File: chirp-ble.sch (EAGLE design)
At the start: 29 parts, among them Q1 ILCX13-FF5F18-32.0000, U1 NRF52832, Y1 ABS07-32.768KHZ-7

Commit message: Fully routed
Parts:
- added TP4: TPB1,27, testpad:TPB1,27
- Q1: value ILCX13-FF5F18-32.0000 -> ILCX13-FF5F18-32.0000
- S1: value SWITCH-MOMENTARY-2-SMD-1101NE -> SWITCH-MOMENTARY-2SMD-1101NE; device SparkFun-Electromechanical:SWITCH-MOMENTARY-2-SMD-1101NE -> SparkFun-Electromechanical:SWITCH-MOMENTARY-2SMD-1101NE
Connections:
- net LED renamed LED_K
- removed net N$14: SWD.SWO
- removed net N$5: SWD.VTREF
- new net LED_A: LED1.A, U1.NFC2/P0.10
- net GND: now also Q1.G1, Q1.G2, TP4.TP, U1.VSS@3
- net VCC: now also SWD.VTREF; no longer LED1.A
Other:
- moved on the sheet: ANTENNA, C1, C10, C11, C12, C13, C2, C3, C5, C6, C7, C8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

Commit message: DRC and ERC
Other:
- moved on the sheet: C9
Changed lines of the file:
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@@
 </instance>
 <instance part="GND8" gate="1" x="152.4" y="43.18"/>
-<instance part="C9" gate="G$1" x="139.7" y="22.86" rot="MR180"/>
+<instance part="C9" gate="G$1" x="147.32" y="22.86" rot="MR180"/>
 <instance part="C10" gate="G$1" x="170.18" y="66.04" smashed="yes" rot="MR270">
 <attribute name="NAME" x="173.736" y="71.501" size="1.778" layer="95" rot="MR0"/>
@@
 <attribute name="NAME" x="183.642" y="20.32" size="1.778" layer="95" rot="MR90"/>
 </instance>
-<instance part="GND10" gate="1" x="139.7" y="15.24"/>
-<instance part="GND11" gate="1" x="170.18" y="17.78"/>
+<instance part="GND10" gate="1" x="147.32" y="15.24"/>
+<instance part="GND11" gate="1" x="170.18" y="15.24"/>
 <instance part="GND13" gate="1" x="177.8" y="45.72"/>
 <instance part="GND16" gate="1" x="127" y="10.16" rot="R90"/>
@@
 <pinref part="GND10" gate="1" pin="GND"/>
 <pinref part="C9" gate="G$1" pin="1"/>
-<wire x1="139.7" y1="17.78" x2="139.7" y2="20.32" width="0.1524" layer="91"/>
+<wire x1="147.32" y1="17.78" x2="147.32" y2="20.32" width="0.1524" layer="91"/>
 </segment>
 <segment>
@@
 <pinref part="GND11" gate="1" pin="GND"/>
 <wire x1="175.26" y1="25.4" x2="170.18" y2="25.4" width="0.1524" layer="91"/>
-<wire x1="170.18" y1="25.4" x2="170.18" y2="20.32" width="0.1524" layer="91"/>
+<wire x1="170.18" y1="25.4" x2="170.18" y2="17.78" width="0.1524" layer="91"/>
 </segment>
 <segment>
@@
 <wire x1="124.46" y1="45.72" x2="132.08" y2="45.72" width="0.1524" layer="91"/>
 <wire x1="132.08" y1="45.72" x2="132.08" y2="43.18" width="0.1524" layer="91"/>
-<wire x1="132.08" y1="43.18" x2="139.7" y2="43.18" width="0.1524" layer="91"/>
-<wire x1="139.7" y1="43.18" x2="139.7" y2="27.94" width="0.1524" layer="91"/>
+<wire x1="132.08" y1="43.18" x2="147.32" y2="43.18" width="0.1524" layer="91"/>
+<wire x1="147.32" y1="43.18" x2="147.32" y2="27.94" width="0.1524" layer="91"/>
 <pinref part="C9" gate="G$1" pin="2"/>
-<wire x1="139.7" y1="27.94" x2="154.94" y2="27.94" width="0.1524" layer="91"/>
-<junction x="139.7" y="27.94"/>
+<wire x1="147.32" y1="27.94" x2="154.94" y2="27.94" width="0.1524" layer="91"/>
+<junction x="147.32" y="27.94"/>
 <pinref part="L1" gate="G$1" pin="1"/>
 </segment>
@@
 <pinref part="U1" gate="G$1" pin="SWDCLK"/>
 <wire x1="124.46" y1="33.02" x2="129.54" y2="33.02" width="0.1524" layer="91"/>
-<label x="124.46" y="33.02" size="1.27" layer="95"/>
+<label x="129.54" y="33.02" size="1.27" layer="95" xref="yes"/>
 </segment>
 </net>
@@
 <pinref part="U1" gate="G$1" pin="SWDIO"/>
 <wire x1="124.46" y1="35.56" x2="129.54" y2="35.56" width="0.1524" layer="91"/>
-<label x="124.46" y="35.56" size="1.27" layer="95"/>
+<label x="129.54" y="35.56" size="1.27" layer="95" xref="yes"/>
 </segment>
 </net>
@@
 <pinref part="U1" gate="G$1" pin="P0.21/RESET"/>
 <wire x1="104.14" y1="15.24" x2="104.14" y2="10.16" width="0.1524" layer="91"/>
+<wire x1="104.14" y1="10.16" x2="106.68" y2="10.16" width="0.1524" layer="91"/>
+<label x="106.68" y="10.16" size="1.27" layer="95" xref="yes"/>
 </segment>
 </net>
@@
 <segment>
 <pinref part="U1" gate="G$1" pin="P0.13"/>
-<wire x1="83.82" y1="15.24" x2="83.82" y2="7.62" width="0.1524" layer="91"/>
-<label x="83.82" y="7.62" size="1.778" layer="95" rot="R90"/>
+<wire x1="83.82" y1="15.24" x2="83.82" y2="10.16" width="0.1524" layer="91"/>
+<label x="83.82" y="10.16" size="1.27" layer="95" rot="R270" xref="yes"/>
 </segment>
 </net>
@@
 <segment>
 <pinref part="U1" gate="G$1" pin="P0.28/AIN4"/>
-<wire x1="96.52" y1="81.28" x2="96.52" y2="93.98" width="0.1524" layer="91"/>
-<label x="96.52" y="83.82" size="1.778" layer="95" rot="R90"/>
+<wire x1="96.52" y1="81.28" x2="96.52" y2="86.36" width="0.1524" layer="91"/>
+<label x="96.52" y="86.36" size="1.27" layer="95" rot="R90" xref="yes"/>
 </segment>
 </net>
@@
 <segment>
 <pinref part="U1" gate="G$1" pin="P0.26"/>
-<wire x1="101.6" y1="81.28" x2="101.6" y2="93.98" width="0.1524" layer="91"/>
+<wire x1="101.6" y1="81.28" x2="101.6" y2="86.36" width="0.1524" layer="91"/>
+<label x="101.6" y="86.36" size="1.27" layer="95" rot="R90" xref="yes"/>
 </segment>
 </net>
@@
 <segment>
 <pinref part="U1" gate="G$1" pin="P0.17"/>
-<wire x1="93.98" y1="15.24" x2="93.98" y2="2.54" width="0.1524" layer="91"/>
-<label x="93.98" y="5.08" size="1.778" layer="95" rot="R90"/>
-</segment>
-</net>
+<wire x1="93.98" y1="15.24" x2="93.98" y2="10.16" width="0.1524" layer="91"/>
+<label x="93.98" y="10.16" size="1.27" layer="95" rot="R270" xref="yes"/>
+</segment>
+</net>

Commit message: Spike
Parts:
- Q1: value ILCX13-FF5F18-32.0000 -> YIC 32.00M-SMDXT324
- Y1: value ABS07-32.768KHZ-7 -> 32.768K-CFPX217
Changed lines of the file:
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@@
 <layer number="251" name="SMDround" color="12" fill="11" visible="no" active="no"/>
 <layer number="254" name="cooling" color="7" fill="1" visible="no" active="yes"/>
+<layer number="255" name="routoute" color="7" fill="1" visible="yes" active="yes"/>
 </layers>
 <schematic xreflabel="%F%N/%S.%C%R" xrefpart="/%S.%C%R">
@@
 <part name="C13" library="rcl" deviceset="C-EU" device="C0402" value="12pF"/>
 <part name="FRAME1" library="frames" deviceset="A4L-LOC" device=""/>
-<part name="Y1" library="abracon" deviceset="CRYSTAL" device=".ABS07" value="ABS07-32.768KHZ-7 "/>
+<part name="Y1" library="abracon" deviceset="CRYSTAL" device=".ABS07" value="32.768K-CFPX217"/>
 <part name="GND9" library="SparkFun" deviceset="GND" device=""/>
-<part name="Q1" library="adafruit" deviceset="XTAL-4" device="-3225" value="ILCX13-FF5F18-32.0000"/>
+<part name="Q1" library="adafruit" deviceset="XTAL-4" device="-3225" value=" YIC 32.00M-SMDXT324 "/>
 <part name="TP1" library="testpad" deviceset="TP" device="B1,27" value="TPB1,27"/>
 <part name="TP2" library="testpad" deviceset="TP" device="B1,27" value="TPB1,27"/>
@@
 <instance part="C11" gate="G$1" x="170.18" y="50.8" smashed="yes" rot="MR270">
 <attribute name="NAME" x="173.736" y="46.101" size="1.778" layer="95" rot="MR0"/>
-<attribute name="VALUE" x="169.164" y="45.339" size="1.778" layer="96" rot="MR180"/>
+<attribute name="VALUE" x="173.736" y="43.561" size="1.778" layer="96" rot="MR0"/>
 </instance>
 <instance part="C12" gate="G$1" x="25.4" y="63.5" smashed="yes" rot="MR90">
@@
 <instance part="GND9" gate="1" x="17.78" y="48.26"/>
 <instance part="Q1" gate="G$1" x="165.1" y="58.42" smashed="yes" rot="R90">
-<attribute name="NAME" x="161.29" y="55.88" size="1.27" layer="95" font="vector" rot="R90"/>
-<attribute name="VALUE" x="170.18" y="54.61" size="1.27" layer="96" font="vector" rot="R90"/>
+<attribute name="NAME" x="162.052" y="53.086" size="1.27" layer="95" font="vector"/>
+<attribute name="VALUE" x="159.004" y="47.752" size="1.27" layer="96" font="vector" rot="R90"/>
 </instance>
 <instance part="L1" gate="G$1" x="162.56" y="27.94" smashed="yes">
@@
 <instance part="GND10" gate="1" x="147.32" y="15.24"/>
 <instance part="GND11" gate="1" x="170.18" y="15.24"/>
-<instance part="GND13" gate="1" x="177.8" y="45.72"/>
+<instance part="GND13" gate="1" x="182.88" y="45.72"/>
 <instance part="GND16" gate="1" x="127" y="10.16" rot="R90"/>
 </instances>
@@
 <pinref part="C10" gate="G$1" pin="2"/>
 <pinref part="GND13" gate="1" pin="GND"/>
-<wire x1="175.26" y1="66.04" x2="177.8" y2="66.04" width="0.1524" layer="91"/>
-<wire x1="177.8" y1="66.04" x2="177.8" y2="63.5" width="0.1524" layer="91"/>
+<wire x1="175.26" y1="66.04" x2="182.88" y2="66.04" width="0.1524" layer="91"/>
+<wire x1="182.88" y1="66.04" x2="182.88" y2="63.5" width="0.1524" layer="91"/>
 <pinref part="C11" gate="G$1" pin="2"/>
-<wire x1="177.8" y1="63.5" x2="177.8" y2="53.34" width="0.1524" layer="91"/>
-<wire x1="177.8" y1="53.34" x2="177.8" y2="50.8" width="0.1524" layer="91"/>
-<wire x1="177.8" y1="50.8" x2="177.8" y2="48.26" width="0.1524" layer="91"/>
-<wire x1="175.26" y1="50.8" x2="177.8" y2="50.8" width="0.1524" layer="91"/>
-<junction x="177.8" y="50.8"/>
+<wire x1="182.88" y1="63.5" x2="182.88" y2="53.34" width="0.1524" layer="91"/>
+<wire x1="182.88" y1="53.34" x2="182.88" y2="50.8" width="0.1524" layer="91"/>
+<wire x1="182.88" y1="50.8" x2="182.88" y2="48.26" width="0.1524" layer="91"/>
+<wire x1="175.26" y1="50.8" x2="182.88" y2="50.8" width="0.1524" layer="91"/>
+<junction x="182.88" y="50.8"/>
 <pinref part="Q1" gate="G$1" pin="G2"/>
-<wire x1="172.72" y1="63.5" x2="177.8" y2="63.5" width="0.1524" layer="91"/>
-<junction x="177.8" y="63.5"/>
+<wire x1="172.72" y1="63.5" x2="182.88" y2="63.5" width="0.1524" layer="91"/>
+<junction x="182.88" y="63.5"/>
 <pinref part="Q1" gate="G$1" pin="G1"/>
-<wire x1="172.72" y1="53.34" x2="177.8" y2="53.34" width="0.1524" layer="91"/>
-<junction x="177.8" y="53.34"/>
-</segment>
-<segment>
+<wire x1="172.72" y1="53.34" x2="182.88" y2="53.34" width="0.1524" layer="91"/>
+<junction x="182.88" y="53.34"/>
+</segment>
+<segment>

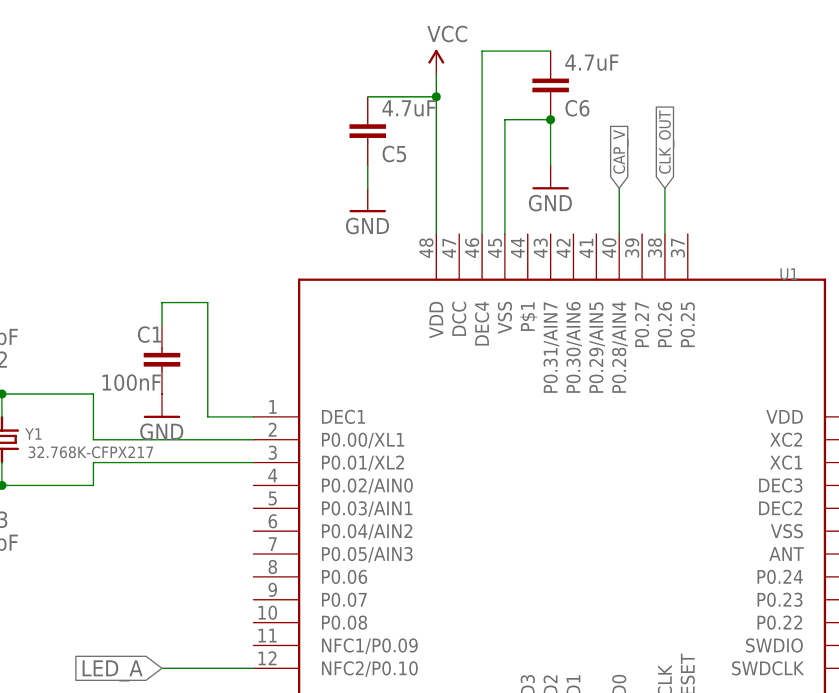
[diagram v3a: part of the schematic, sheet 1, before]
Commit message: Changed min drill size to 0.4mm
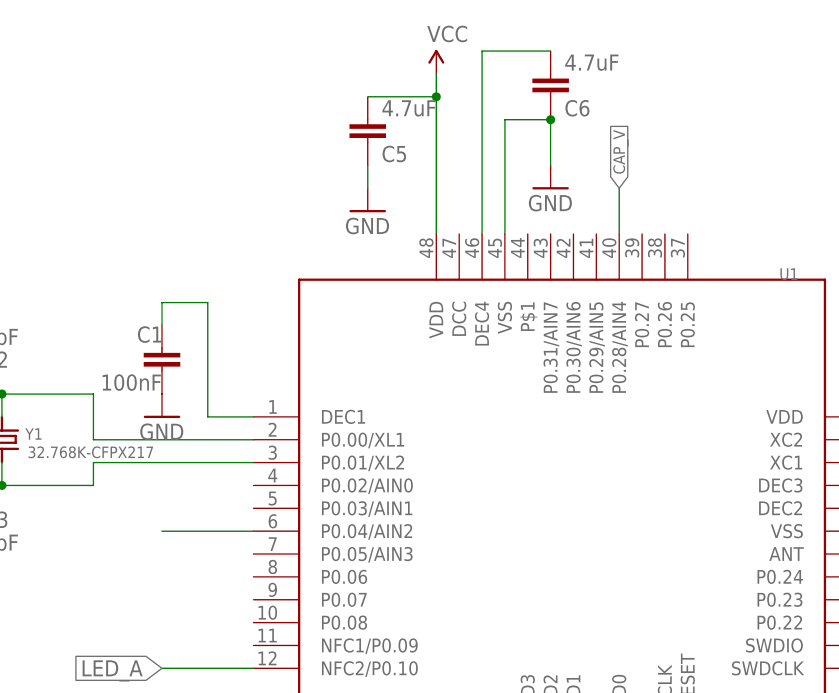
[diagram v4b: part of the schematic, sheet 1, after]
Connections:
- net CLK_OUT: now also U1.P0.04/AIN2; no longer U1.P0.26
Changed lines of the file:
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@@
-</segment>
-</net>
-<net name="CLK_OUT" class="0">
-<segment>
-<pinref part="U1" gate="G$1" pin="P0.26"/>
-<wire x1="101.6" y1="81.28" x2="101.6" y2="86.36" width="0.1524" layer="91"/>
-<label x="101.6" y="86.36" size="1.27" layer="95" rot="R90" xref="yes"/>
 </segment>
 </net>
@@
 </segment>
 </net>
+<net name="CLK_OUT" class="0">
+<segment>
+<pinref part="U1" gate="G$1" pin="P0.04/AIN2"/>
+<wire x1="55.88" y1="48.26" x2="45.72" y2="48.26" width="0.1524" layer="91"/>
+</segment>
+</net>
